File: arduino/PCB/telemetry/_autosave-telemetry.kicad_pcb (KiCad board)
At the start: 2 copper layers, 3 parts, among them U1 MEGA_PRO_EMBED_CH340G_{slash}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, U2 NEO-M8N

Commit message: Agregando objeto laps
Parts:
- added J1: Boton Enter, Button_Switch_SMD:SW_SPST_EVPBF, F.Cu at (91.4, 106.7)
- added J3: Boton Next, Button_Switch_SMD:SW_SPST_EVPBF, F.Cu at (106.7, 106.7)
- added R1: R_Photo, Resistor_THT:R_Axial_DIN0204_L3.6mm_D1.6mm_P7.62mm_Horizontal, F.Cu at (123.2, 109.2)
- added R2: R_Photo, Resistor_THT:R_Axial_DIN0204_L3.6mm_D1.6mm_P7.62mm_Horizontal, F.Cu at (77.5, 109.2)
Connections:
- U1 pad D2: unconnected-(U1-PadD2) -> Net-(J3-Pin_1)
- U1 pad D3: unconnected-(U1-PadD3) -> Net-(J1-Pin_2)
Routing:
- net unconnected-(U2-D_SEL-Pad2): track 20.2 -> 101.1 mm
- net RX_GPS: track 45.4 -> 55.9 mm
- net Net-(J1-Pin_2): track 0.00 -> 3.69 mm

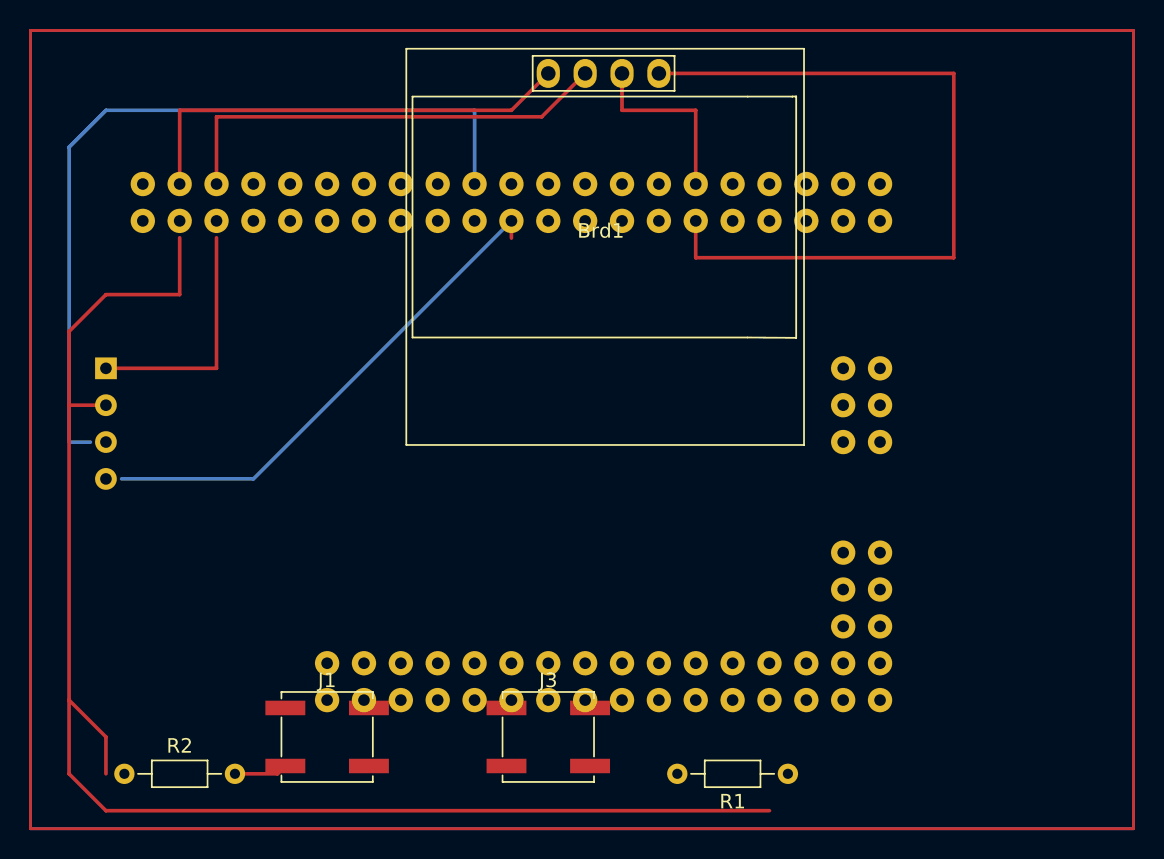
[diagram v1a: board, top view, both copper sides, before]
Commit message: Add Feature of Revolutions
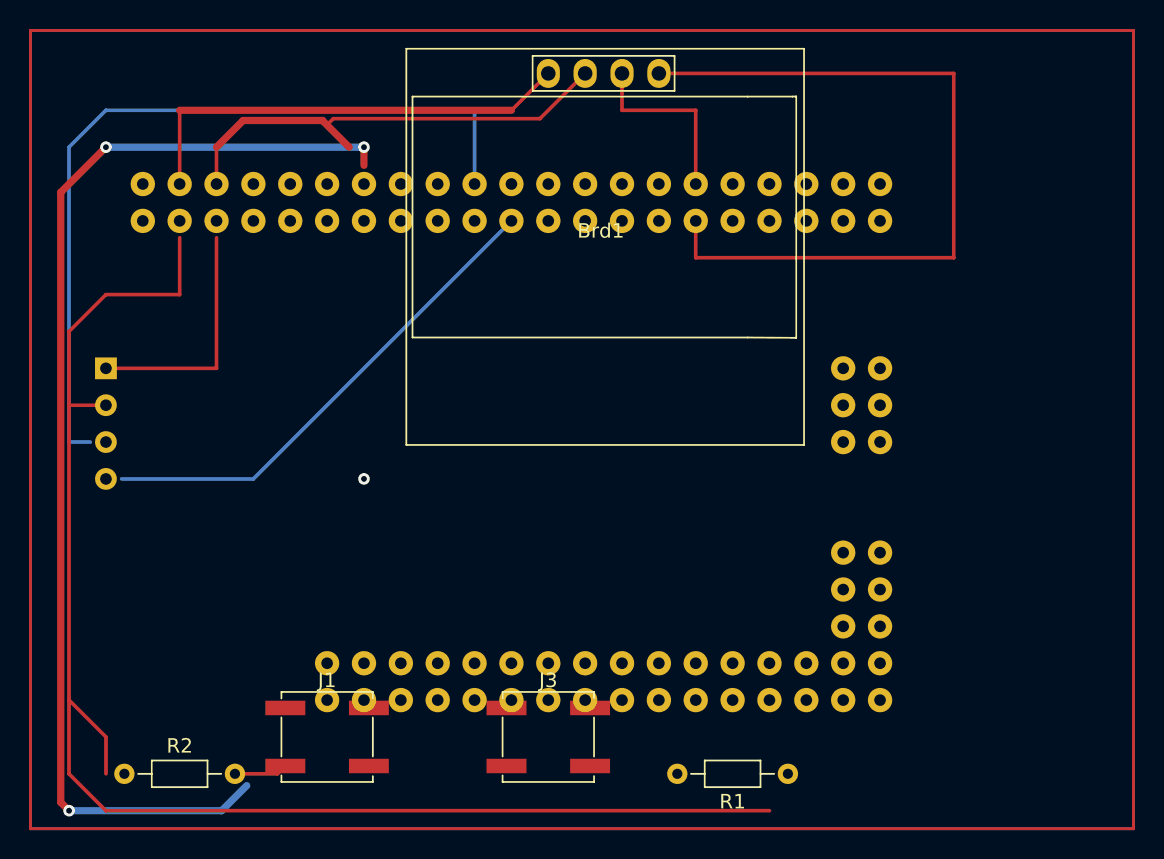
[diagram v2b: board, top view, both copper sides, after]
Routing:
- net (no net): track 0.00 -> 79.2 mm, vias 0 -> 4
- net +5V: track 31.3 -> 34.6 mm
- net DX_GPS: track 35.4 -> 34.2 mm
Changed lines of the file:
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@@
         (effects (font (size 1 1) (thickness 0.15)))
     )
-    (fp_text value "SSD1306" (at -7.747 -7.62) (layer "F.Fab")
+    (fp_text value "SSD1306" (at -7.747 -7.62) (layer "F.Fab") hide
         (effects (font (size 1 1) (thickness 0.15)))
     )
@@
         (effects (font (size 1 1) (thickness 0.15)) (justify mirror))
     )
-    (fp_text value "MEGA_PRO_EMBED_CH340G_{slash}_ATMEGA2560" (at -0.435 -20.955) (layer "B.Fab")
+    (fp_text value "MEGA_PRO_EMBED_CH340G_{slash}_ATMEGA2560" (at -0.435 -20.955) (layer "B.Fab") hide
         (effects (font (size 1 1) (thickness 0.15)) (justify mirror))
     )
@@
   (gr_rect (start 71 58) (end 147 113)
     (stroke (width 0.2) (type default)) (fill none) (layer "B.Cu"))
+  (segment (start 93.98 66.04) (end 93.98 67.2918) (width 0.5) (layer "F.Cu") (net 0))
+  (segment (start 73.085 69.155) (end 73.085 111.185) (width 0.5) (layer "F.Cu") (net 0))
+  (segment (start 76.2 66.04) (end 73.085 69.155) (width 0.5) (layer "F.Cu") (net 0))
+  (segment (start 73.085 111.185) (end 73.66 111.76) (width 0.5) (layer "F.Cu") (net 0))
+  (via (at 73.66 111.76) (size 0.8) (drill 0.4) (layers "F.Cu" "B.Cu") (net 0))
+  (via (at 76.2 66.04) (size 0.8) (drill 0.4) (layers "F.Cu" "B.Cu") (net 0))
+  (via (at 93.98 88.9) (size 0.8) (drill 0.4) (layers "F.Cu" "B.Cu") (net 0))
+  (via (at 93.98 66.04) (size 0.8) (drill 0.4) (layers "F.Cu" "B.Cu") (net 0))
+  (segment (start 84.176346 111.76) (end 85.903173 110.033173) (width 0.5) (layer "B.Cu") (net 0))
+  (segment (start 93.98 66.04) (end 76.2 66.04) (width 0.5) (layer "B.Cu") (net 0))
+  (segment (start 73.66 111.76) (end 84.176346 111.76) (width 0.5) (layer "B.Cu") (net 0))
   (segment (start 104.14 63.5) (end 106.68 60.96) (width 0.25) (layer "F.Cu") (net 2))
   (segment (start 81.28 68.58) (end 81.28 63.5) (width 0.25) (layer "F.Cu") (net 2))
-  (segment (start 81.28 63.5) (end 104.14 63.5) (width 0.25) (layer "F.Cu") (net 2))
-  (segment (start 83.82 68.58) (end 83.82 63.95) (width 0.25) (layer "F.Cu") (net 3))
-  (segment (start 106.23 63.95) (end 109.22 60.96) (width 0.25) (layer "F.Cu") (net 3))
-  (segment (start 83.82 63.95) (end 106.23 63.95) (width 0.25) (layer "F.Cu") (net 3))
+  (segment (start 81.28 63.5) (end 104.14 63.5) (width 0.5) (layer "F.Cu") (net 2))
+  (segment (start 85.66 64.2) (end 83.82 66.04) (width 0.5) (layer "F.Cu") (net 3))
+  (segment (start 91.44 64.525305) (end 91.44 64.499695) (width 0.25) (layer "F.Cu") (net 3))
+  (segment (start 92.954695 66.04) (end 91.44 64.525305) (width 0.25) (layer "F.Cu") (net 3))
+  (segment (start 83.82 68.58) (end 83.82 66.04) (width 0.25) (layer "F.Cu") (net 3))
+  (segment (start 106.105 64.075) (end 109.22 60.96) (width 0.25) (layer "F.Cu") (net 3))
+  (segment (start 91.114695 64.2) (end 85.66 64.2) (width 0.5) (layer "F.Cu") (net 3))
+  (segment (start 91.44 64.499695) (end 91.864695 64.075) (width 0.25) (layer "F.Cu") (net 3))
+  (segment (start 91.864695 64.075) (end 106.105 64.075) (width 0.25) (layer "F.Cu") (net 3))
+  (segment (start 92.954695 66.04) (end 91.114695 64.2) (width 0.5) (layer "F.Cu") (net 3))
   (segment (start 85.09 109.22) (end 88.02 109.22) (width 0.25) (layer "F.Cu") (net 9))
   (segment (start 88.02 109.22) (end 88.56 108.68) (width 0.25) (layer "F.Cu") (net 9))
@@
   (segment (start 111.76 63.5) (end 111.76 60.96) (width 0.25) (layer "F.Cu") (net 18))
   (segment (start 116.84 68.58) (end 116.84 63.5) (width 0.25) (layer "F.Cu") (net 18))
-  (segment (start 104.14 71.12) (end 104.14 72.305393) (width 0.25) (layer "F.Cu") (net 23))
   (segment (start 104.14 71.12) (end 86.36 88.9) (width 0.25) (layer "B.Cu") (net 23))
   (segment (start 86.36 88.9) (end 77.275 88.9) (width 0.25) (layer "B.Cu") (net 23))
